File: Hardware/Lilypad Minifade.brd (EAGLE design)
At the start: 20 x 20 mm, 14 parts, among them U1 ATTINY85

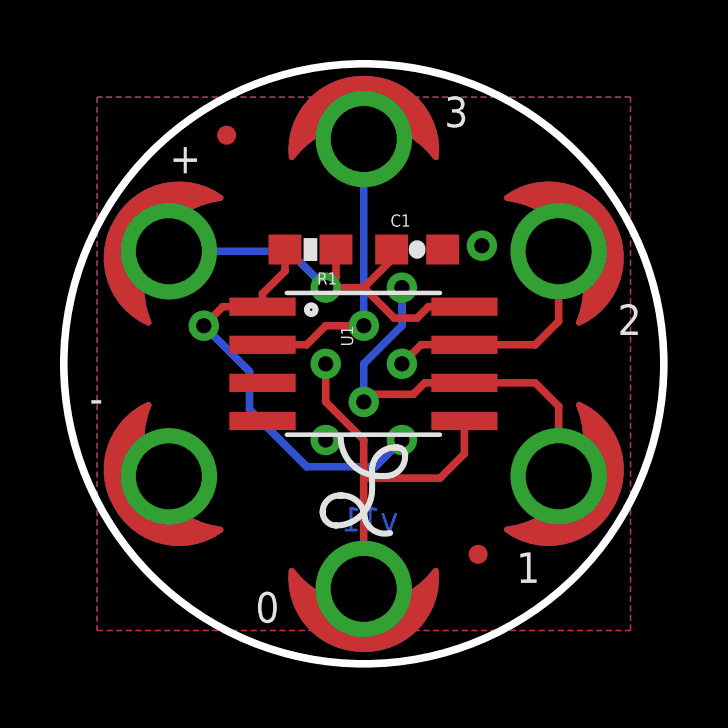
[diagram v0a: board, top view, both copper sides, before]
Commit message: Correcting hardware files to current pcbs we are selling
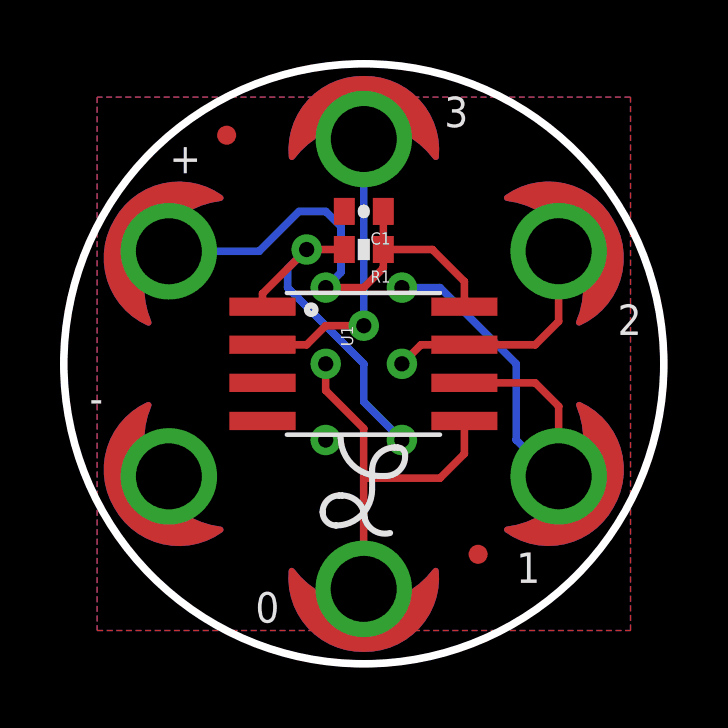
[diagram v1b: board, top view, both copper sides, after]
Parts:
- removed FRAME2: FRAME-LETTER, SparkFun-Aesthetics:CREATIVE_COMMONS
- removed LOGO1: OSHW-LOGOS, SparkFun-Aesthetics:OSHW-LOGO-S
- added U$1: CREATIVE_COMMONS, SparkFun:CREATIVE_COMMONS
- C1: device SparkFun:0603-CAP -> SparkFun:0402-CAP
- R1: device SparkFun:0603-RES -> SparkFun:0402-RES
- moved C1 2.18 mm to (0.00, 5.08), turned to 180 degrees
- moved R1 1.78 mm to (0.00, 3.81)
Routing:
- net N$9: track 0.00 -> 4.86 mm, vias 0 -> 1
- net N$4: track 14.0 -> 10.3 mm, vias 2 -> 0
- net VCC: track 14.0 -> 16.8 mm
- net NRESET: track 14.1 -> 12.0 mm
- net N$3: vias 1 -> 0
- net N$5: vias 1 -> 0
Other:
- board text removed: "Revised by Pete Lewis"
- board text removed: "Tiny"
- board text removed: "Twinkle"
- board text removed: "v11"
